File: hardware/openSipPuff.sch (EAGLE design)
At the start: 26 parts, among them J1 AVR_SPI_PRG_62X3_LOCK, J2 I2C, U1 ATMEGA32U4TQFP, U2 AD8223, U3 MPX12GP, Y1 16MHz

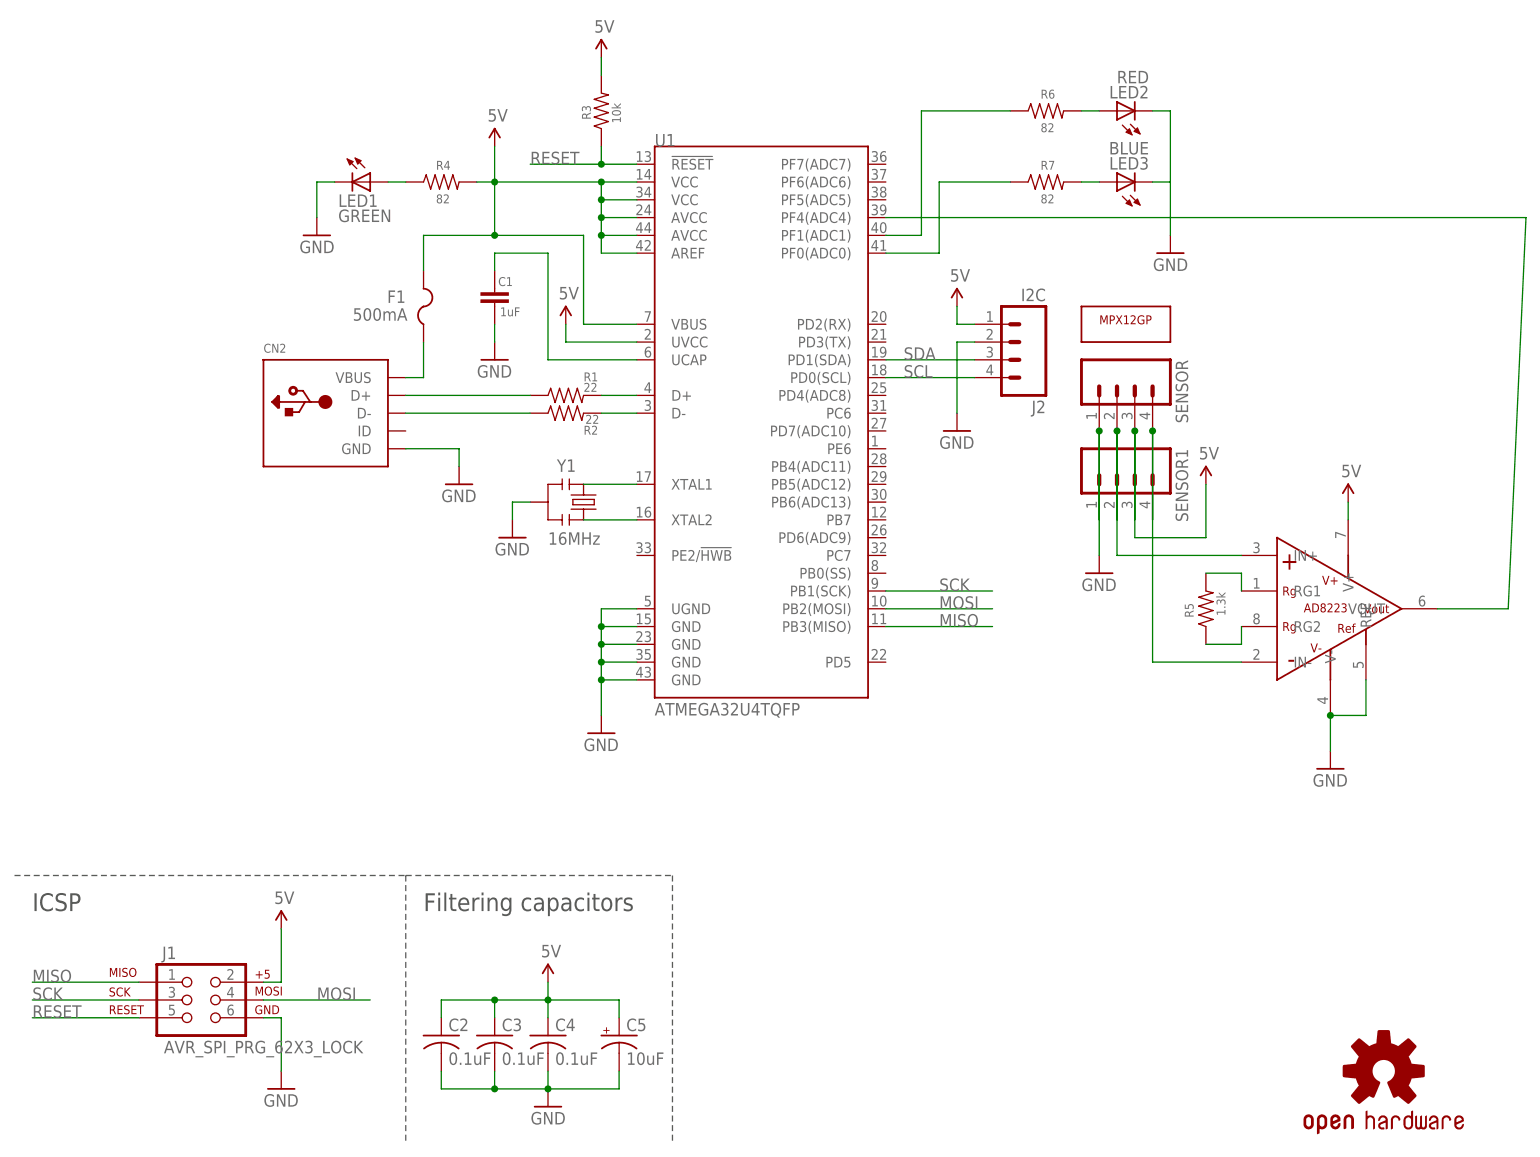
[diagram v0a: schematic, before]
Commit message: Major board updates with new sensor, I2C interface, and more
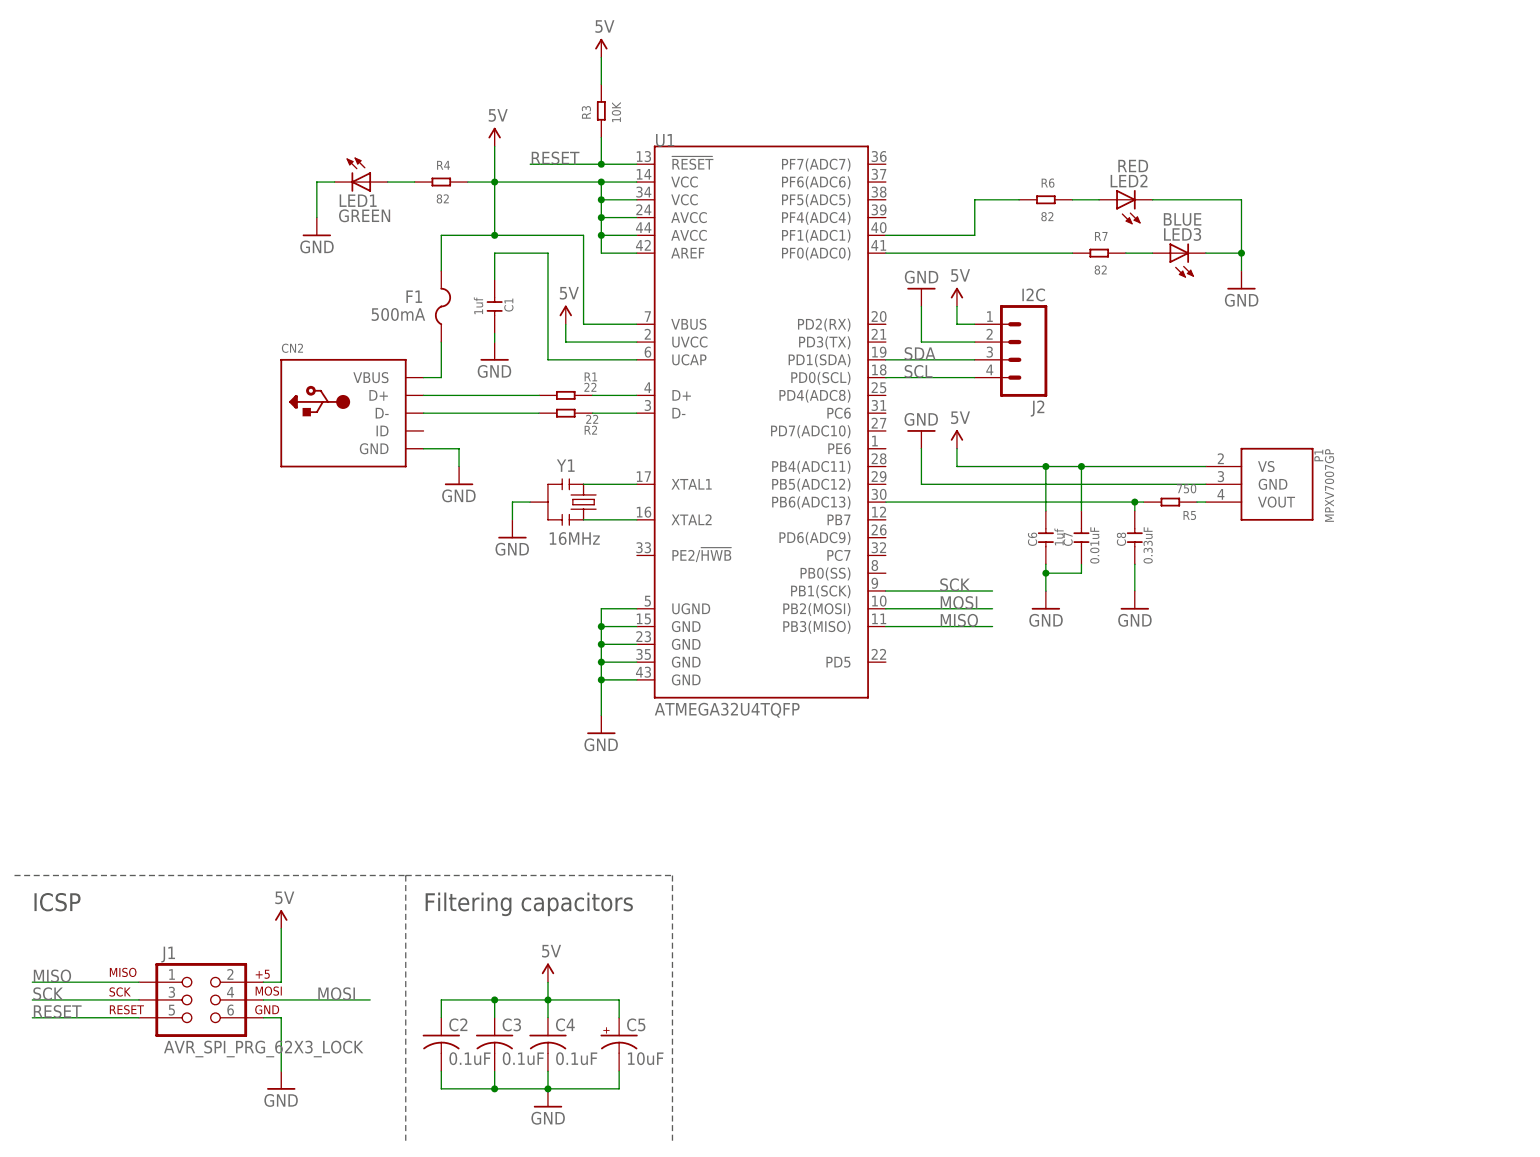
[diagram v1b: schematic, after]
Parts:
- removed LOGO1: OSHW-LOGOL, SparkFun-Aesthetics:OSHW-LOGOL
- removed SENSOR, SENSOR1: (no value), SparkFun-Connectors:M04PTH
- removed U2: AD8223, sip-and-puff:AD8223
- removed U3: MPX12GP, sip-and-puff:MPX12GP
- added C6: 1uf, Seeed-Capacitor:CERAMIC-1UF-25V-10%-X7R(0805)
- added C7: 0.01uF, Seeed-Capacitor:CERAMIC-10NF-50V-5%-X7R(0805)
- added C8: 0.33uF, Seeed-Capacitor:CERAMIC-10NF-50V-5%-X7R(0805)
- added P1: MPXV7007GP, MPXV7007GP:MPXV7007GP
- C1: value 1uF -> 1uf; device SparkFun-Capacitors:CAP0805 -> Seeed-Capacitor:CERAMIC-1UF-25V-10%-X7R(0805)
- R1, R2: device SparkFun-Resistors:RESISTOR0805-RES -> Seeed-OPL-Resistor:RES-0805
- R3: value 10k -> 10K; device SparkFun-Resistors:RESISTOR0805-RES -> Seeed-Resistor:SMD-RES-10K-1%-1/8W(0805)
- R4: device SparkFun-Resistors:RESISTOR0805-RES -> Seeed-Resistor:SMD-RES-0.1R-5%-1/8W(0805)
- R5: value 1.3k -> 750; device SparkFun-Resistors:RESISTOR0805-RES -> Seeed-Resistor:SMD-RES-2.2K-5%-1/8W(0805)
- R6, R7: device SparkFun-Resistors:RESISTOR0805-RES -> Seeed-Resistor:SMD-RES-2.2K-5%-1/8W(0805)
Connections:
- removed net N$11: R5.1, U2.RG2
- removed net N$13: SENSOR.4, SENSOR1.4, U2.IN-
- removed net OUTPUT: U1.PF4(ADC4), U2.VOUT
- net 5V: now also C6.2, C7.2, P1.VS; no longer SENSOR.3, SENSOR1.3, U2.V+
- net GND: now also C6.1, C7.1, C8.1, P1.GND; no longer SENSOR.1, SENSOR1.1, U2.REF, U2.V-
- net N$10: now also P1.VOUT, R5.1; no longer SENSOR.2, SENSOR1.2, U2.IN+
- net N$7: now also C8.2, U1.PB6(ADC13); no longer U2.RG1
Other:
- moved on the sheet: CN2, F1, LED2, LED3
